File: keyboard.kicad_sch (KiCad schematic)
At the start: 1 part, among them U1 RP2040

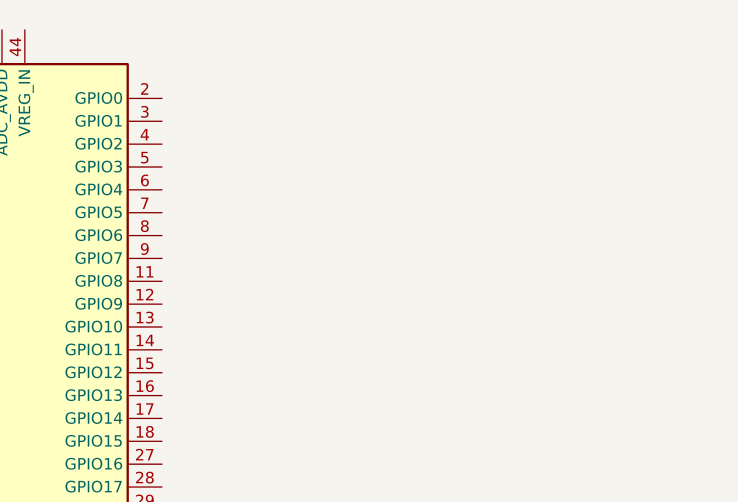
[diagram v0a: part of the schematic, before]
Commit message: Wired rows and columns and added i2c pinheader
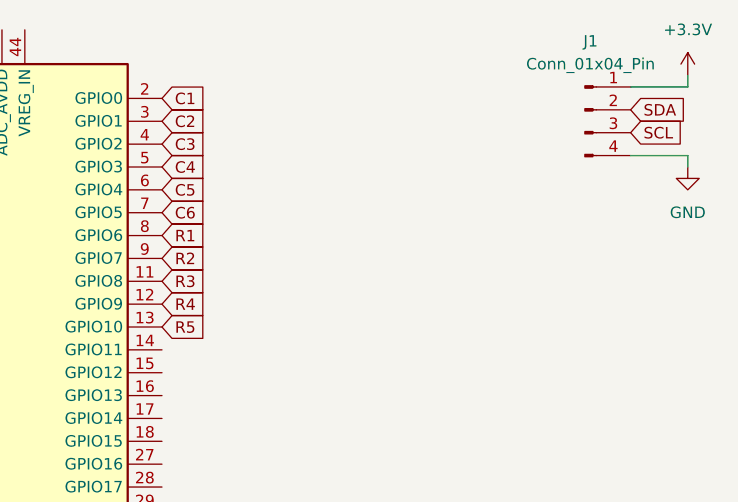
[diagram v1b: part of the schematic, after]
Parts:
- added J1: Conn_01x04_Pin, Connector_PinHeader_2.54mm:PinHeader_1x04_P2.54mm_Vertical, symbol Connector:Conn_01x04_Pin
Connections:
- net R3: now reaches U1.11 (GPIO8)
- net R4: now reaches U1.12 (GPIO9)
- net R5: now reaches U1.13 (GPIO10)
- net C1: now reaches U1.2 (GPIO0)
- net C2: now reaches U1.3 (GPIO1)
- net C3: now reaches U1.4 (GPIO2)
- net C4: now reaches U1.5 (GPIO3)
- net C5: now reaches U1.6 (GPIO4)
- net C6: now reaches U1.7 (GPIO5)
- net R1: now reaches U1.8 (GPIO6)
- net R2: now reaches U1.9 (GPIO7)
- new net +3.3V: J1.1 (Pin_1)
- new net GND: J1.4 (Pin_4)
- new net SCL: J1.3 (Pin_3)
- new net SDA: J1.2 (Pin_2)

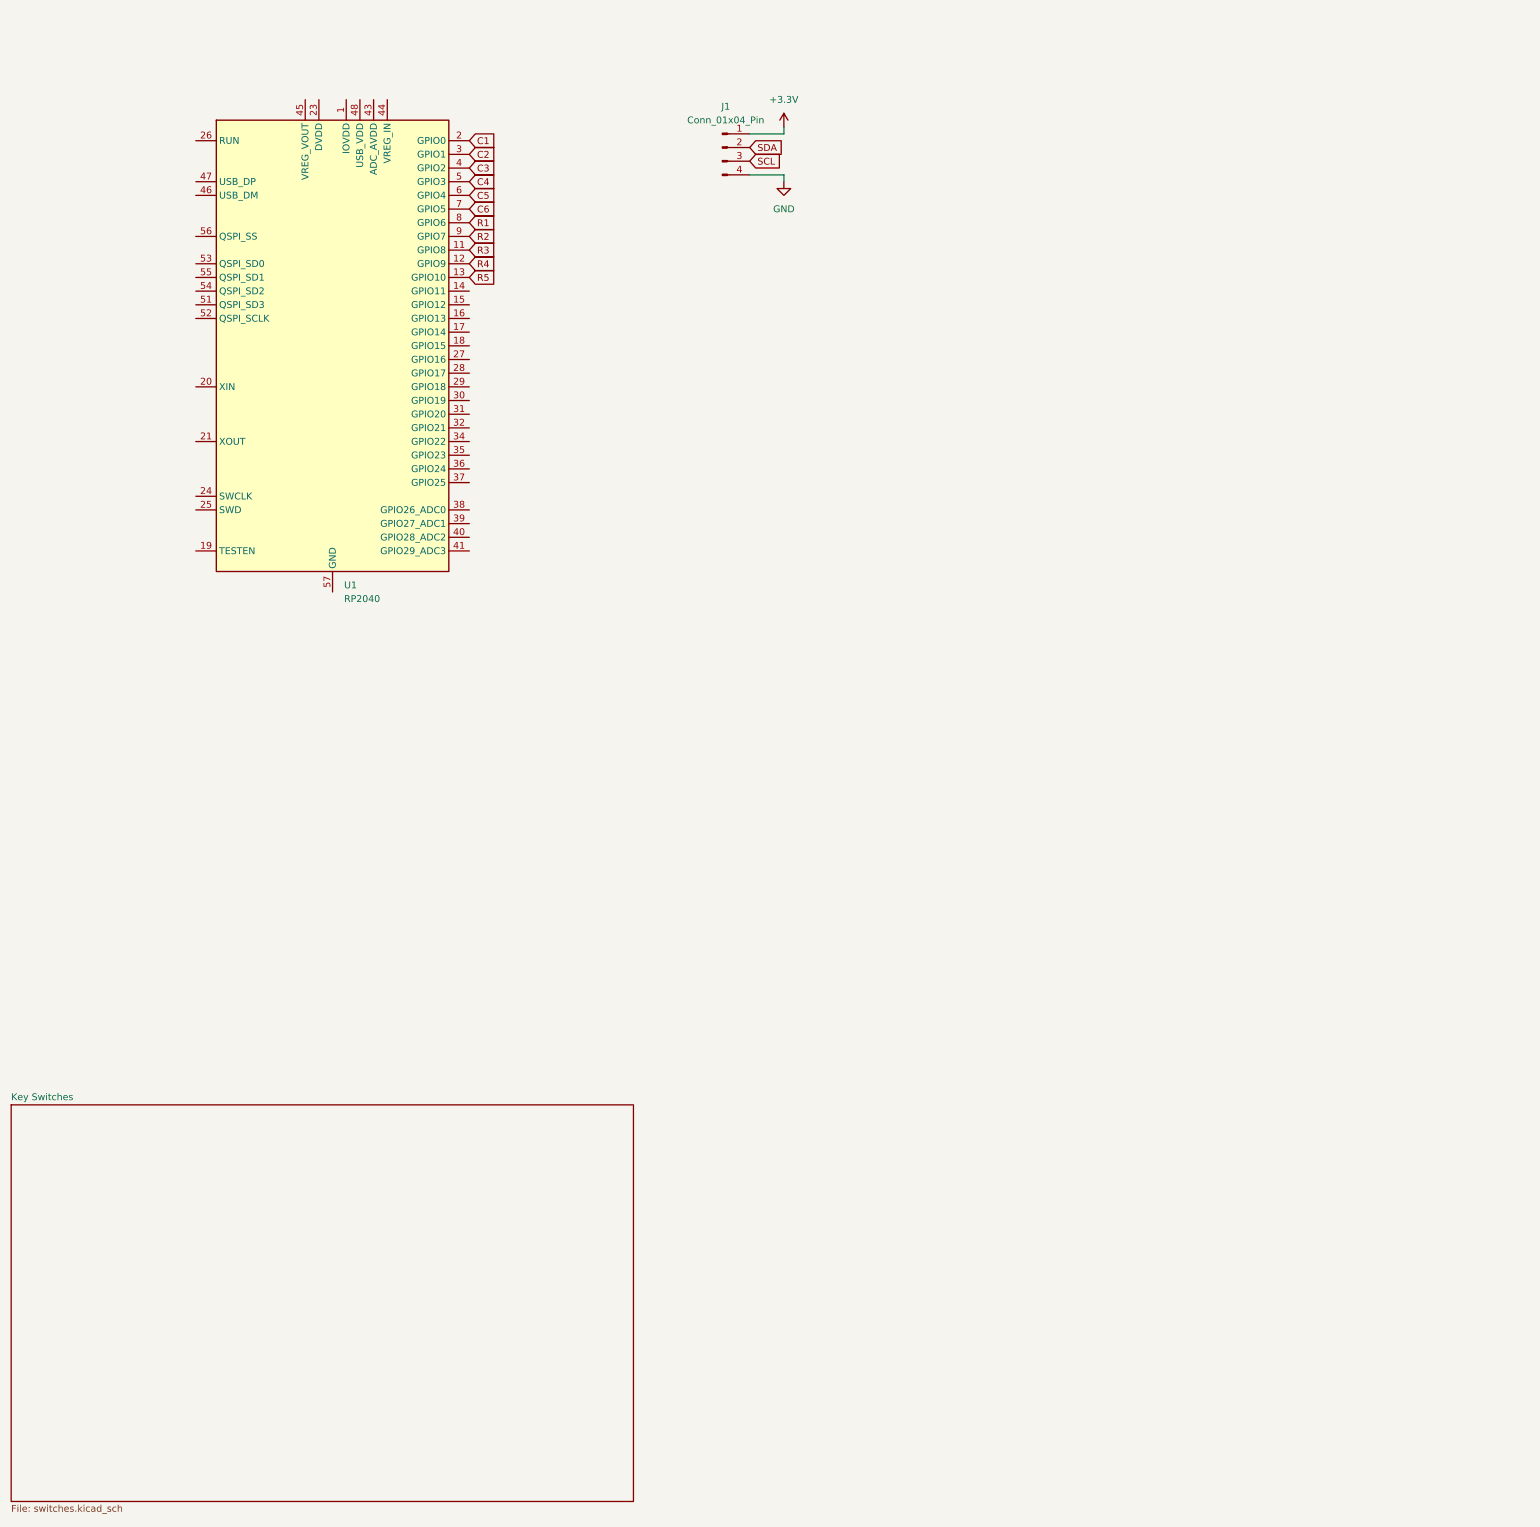
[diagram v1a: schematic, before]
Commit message: More wiring for the RP2040
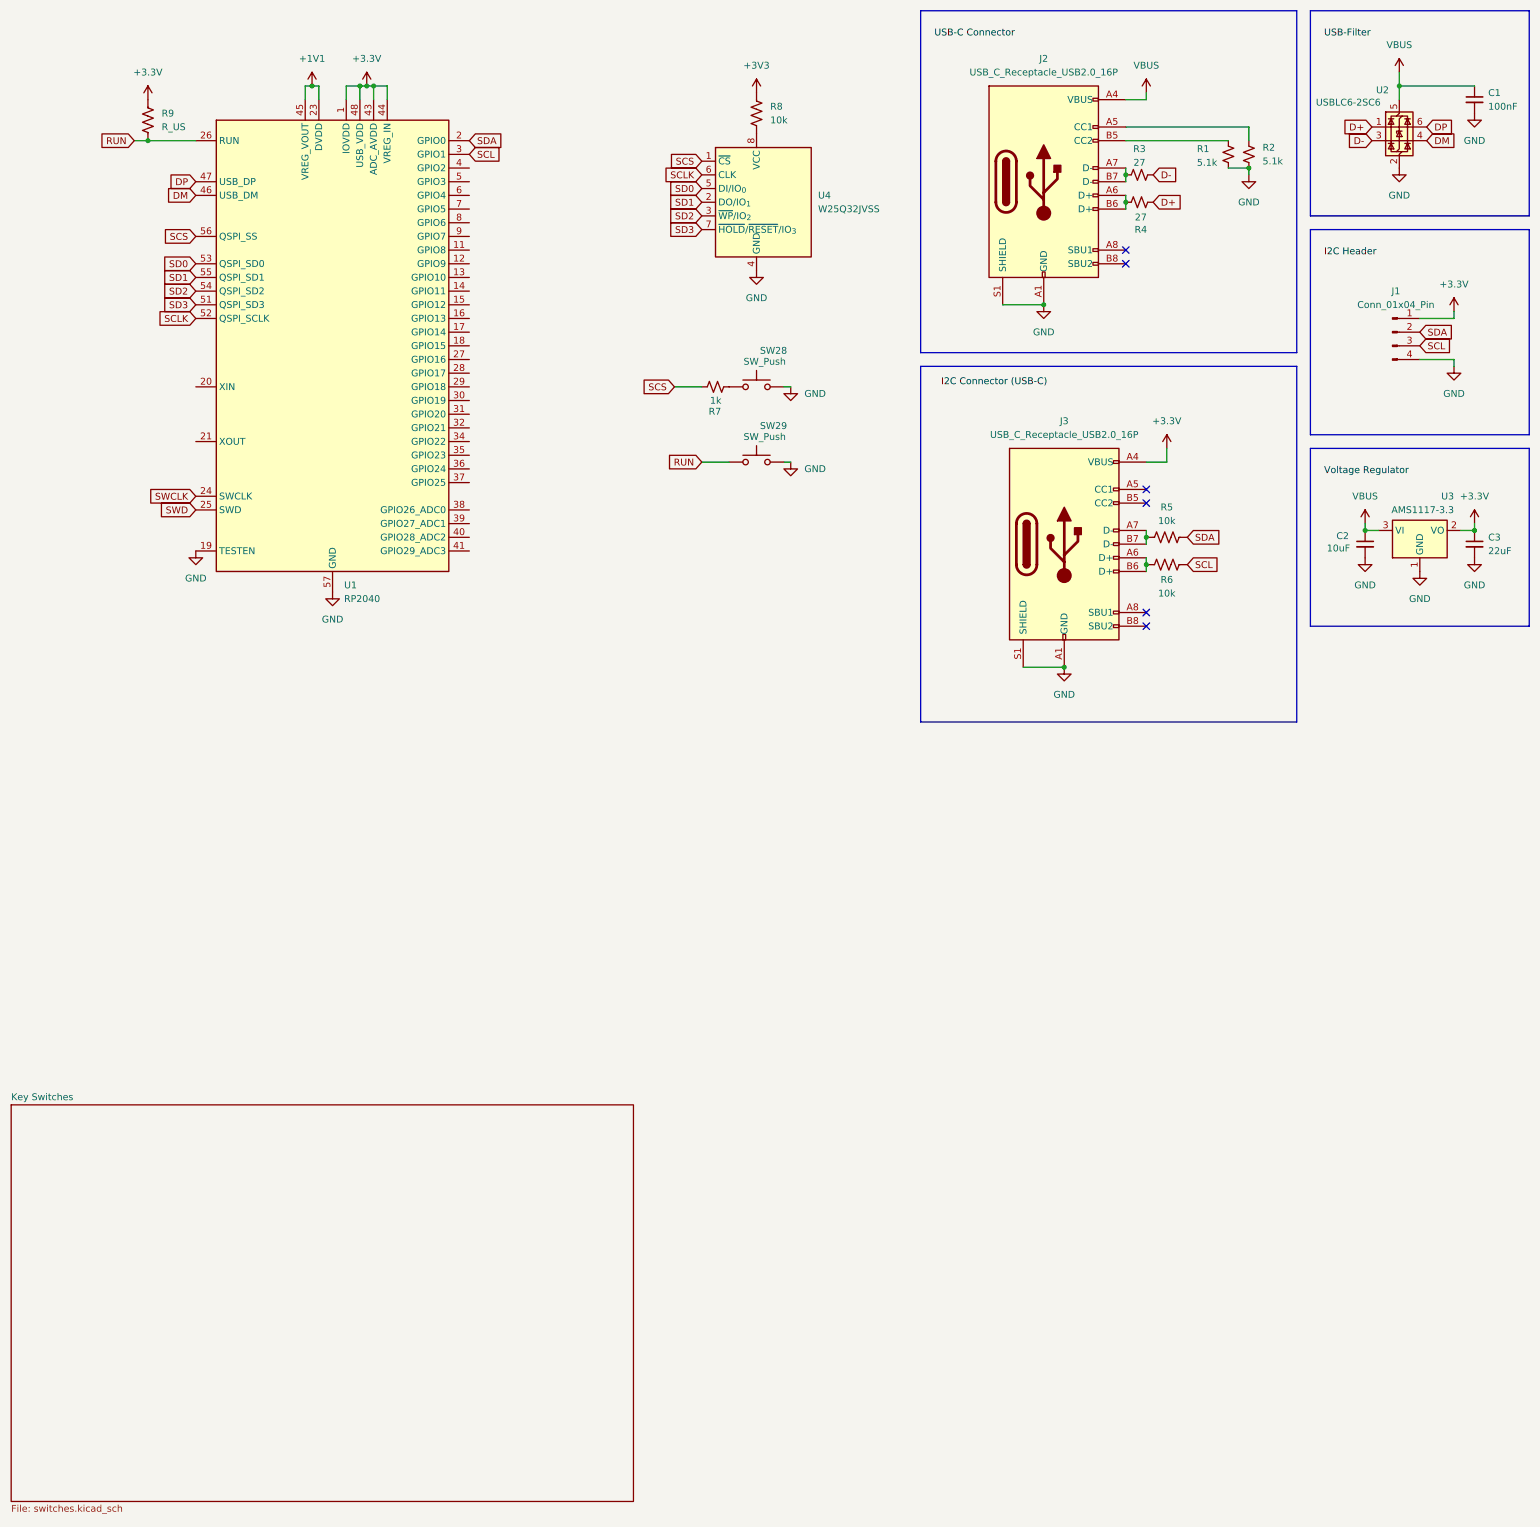
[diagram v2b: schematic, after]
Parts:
- added C1: 100nF, symbol Device:C_Small
- added C2: 10uF, symbol Device:C_Small
- added C3: 22uF, symbol Device:C_Small
- added J2, J3: USB_C_Receptacle_USB2.0_16P, symbol Connector:USB_C_Receptacle_USB2.0_16P
- added R1, R2: 5.1k, symbol Device:R_Small_US
- added R3, R4: 27, symbol Device:R_Small_US
- added R5, R6, R8: 10k, symbol Device:R_US
- added R7: 1k, symbol Device:R_Small_US
- added R9: R_US, symbol Device:R_US
- added SW28, SW29: SW_Push, symbol Switch:SW_Push
- added U2: USBLC6-2SC6, Package_TO_SOT_SMD:SOT-23-6, symbol Power_Protection:USBLC6-2SC6
- added U3: AMS1117-3.3, Package_TO_SOT_SMD:SOT-223-3_TabPin2, symbol Regulator_Linear:AMS1117-3.3
- added U4: W25Q32JVSS, Package_SO:SOIC-8_5.3x5.3mm_P1.27mm, symbol Memory_Flash:W25Q32JVSS
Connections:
- net C1 is gone; now on net SDA: U1.2 (GPIO0)
- net C2 is gone; now on net SCL: U1.3 (GPIO1)
- net +3.3V: now also U1.1 (IOVDD), U1.10 (IOVDD), U1.22 (IOVDD), U1.33 (IOVDD), U1.42 (IOVDD), U1.43 (ADC_AVDD), U1.44 (VREG_IN), U1.48 (USB_VDD), U1.49 (IOVDD), C3.1, J3.A4 (VBUS), J3.A9 (VBUS), J3.B4 (VBUS), J3.B9 (VBUS), R9.1, U3.2 (VO)
- net GND: now also U1.19 (TESTEN), U1.57 (GND), C1.2, C2.2, C3.2, J2.A1 (GND), J2.A12 (GND), J2.B1 (GND), J2.B12 (GND), J2.S1 (SHIELD), J3.A1 (GND), J3.A12 (GND), J3.B1 (GND), J3.B12 (GND), J3.S1 (SHIELD), R1.2, R2.2, SW28.2, SW29.2, U2.2 (GND), U3.1 (GND), U4.4 (GND)
- net SCL: now also R6.1
- net SDA: now also R5.1
- net +1V1: now reaches U1.23 (DVDD), U1.50 (DVDD)
- net +1V1: now also U1.45 (VREG_VOUT)
- net SWCLK: now reaches U1.24 (SWCLK)
- net SWD: now reaches U1.25 (SWD)
- net RUN: now reaches U1.26 (RUN)
- net RUN: now also R9.2, SW29.1
- net DM: now reaches U1.46 (USB_DM)
- net DM: now also U2.4 (I/O2)
- net DP: now reaches U1.47 (USB_DP)
- net DP: now also U2.6 (I/O1)
- net SD3: now reaches U1.51 (QSPI_SD3)
- net SD3: now also U4.7 (~{HOLD}/~{RESET}/IO_{3})
- net SCLK: now reaches U1.52 (QSPI_SCLK)
- net SCLK: now also U4.6 (CLK)
- net SD0: now reaches U1.53 (QSPI_SD0)
- net SD0: now also U4.5 (DI/IO_{0})
- net SD2: now reaches U1.54 (QSPI_SD2)
- net SD2: now also U4.3 (~{WP}/IO_{2})
- net SD1: now reaches U1.55 (QSPI_SD1)
- net SD1: now also U4.2 (DO/IO_{1})
- net SCS: now reaches U1.56 (QSPI_SS)
- net SCS: now also R7.2, U4.1 (~{CS})
- net C3: no longer names the net of U1.4 (GPIO2)
- net C4: no longer names the net of U1.5 (GPIO3)
- net C5: no longer names the net of U1.6 (GPIO4)
- net C6: no longer names the net of U1.7 (GPIO5)
- net R1: no longer names the net of U1.8 (GPIO6)
- net R2: no longer names the net of U1.9 (GPIO7)
- net R3: no longer names the net of U1.11 (GPIO8)
- net R4: no longer names the net of U1.12 (GPIO9)
- net R5: no longer names the net of U1.13 (GPIO10)
- new net: J3.A6 (D+), J3.B6 (D+), R6.2
- new net: J3.A7 (D-), J3.B7 (D-), R5.2
- new net: J2.A5 (CC1), R2.1
- new net: J2.A6 (D+), J2.B6 (D+), R4.1
- new net: J2.A7 (D-), J2.B7 (D-), R3.1
- new net: J2.B5 (CC2), R1.1
- new net: R7.1, SW28.1
- new net: R8.2, U4.8 (VCC)
- new net +3V3: R8.1
- new net D+: R4.2, U2.1 (I/O1)
- new net D-: R3.2, U2.3 (I/O2)
- new net VBUS: C1.1, C2.1, J2.A4 (VBUS), J2.A9 (VBUS), J2.B4 (VBUS), J2.B9 (VBUS), U2.5 (VBUS), U3.3 (VI)
- no-connect marks 0 -> 6
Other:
- moved on the sheet: J1
